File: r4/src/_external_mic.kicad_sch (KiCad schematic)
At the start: 145 parts, among them J27 , Q12 BSS84PW, Q13 BSS84PW, Q14 NX6008NBKW, Q15 NX3008NBKW, Q16 NX3008NBKW, Q17 NX3008NBKW, Q18 NX3008NBKW, Q19 NX3008NBKW, Q20 BSS84PW, Q21 BSS84PW, Q22 NX3008NBKW, Q23 NX3008NBKW, Q24 NX3008NBKW, Q25 BSS84PW, T17 , T18 , T19 , T20 , T21 , T22 , T23 , T24 , T25 , T26 , T27 , T28 , T29 , T30 , T31 , T32 , T33 , T34 , T35 , T36 , T37 , T38 , T41 , T43 , T44 , T45 , T46 , T47 , T48 , T49 , T50 , U17 74HC20, U18 THAT5173, U19 74HC74, U20 74HC132, U21 74HC4520, U22 74HC132, U23 THAT1580, U24 74HC688, U25 LM4562, U26 74HC688, U27 AD4005

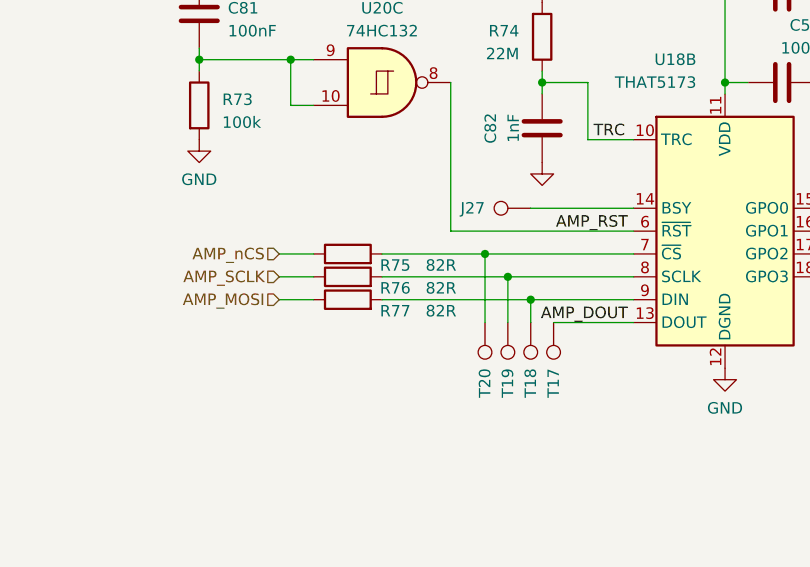
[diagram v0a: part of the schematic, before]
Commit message: Move SPI termination resistors to the source end of the bus (no electrical change, but clearer in schematic
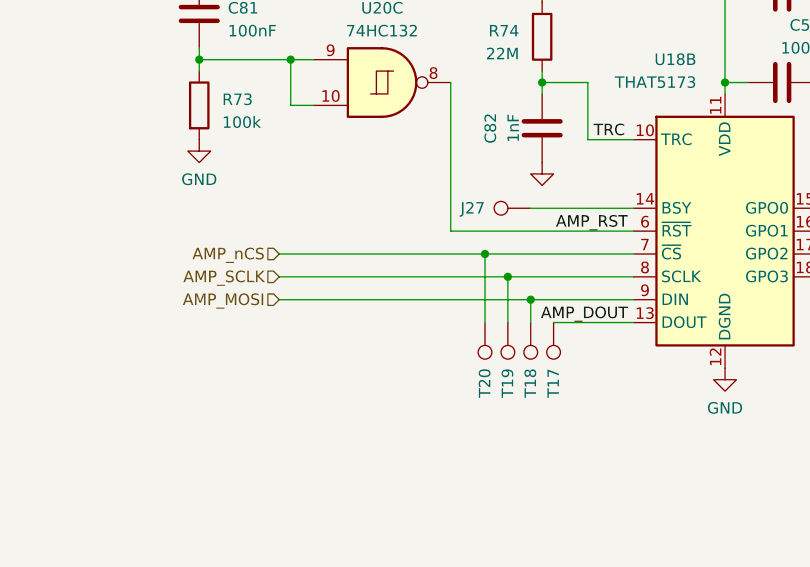
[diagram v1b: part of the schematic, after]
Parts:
- removed R75, R76, R77: 82R, Resistor_SMD:R_0402_1005Metric, symbol Device:R
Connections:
- net AMP_MOSI: now also T18.1, U18.9 (DIN)
- net AMP_SCLK: now also T19.1, U18.8 (SCLK)
- net AMP_nCS: now also T20.1, U18.7 (~{CS})
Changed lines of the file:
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@@
     (stroke (width 0) (type default))
   )
-  (wire (pts (xy 153.67 134.62) (xy 165.1 134.62))
+  (wire (pts (xy 142.24 134.62) (xy 165.1 134.62))
     (stroke (width 0) (type default))
   )
@@
     (stroke (width 0) (type default))
   )
-  (wire (pts (xy 153.67 137.16) (xy 167.64 137.16))
+  (wire (pts (xy 142.24 137.16) (xy 167.64 137.16))
     (stroke (width 0) (type default))
   )
@@
     (stroke (width 0) (type default))
   )
-  (wire (pts (xy 142.24 134.62) (xy 146.05 134.62))
-    (stroke (width 0) (type default))
-  )
   (wire (pts (xy 287.02 63.5) (xy 287.02 68.58))
     (stroke (width 0) (type default))
@@
     (stroke (width 0) (type default))
   )
-  (wire (pts (xy 142.24 137.16) (xy 146.05 137.16))
-    (stroke (width 0) (type default))
-  )
   (wire (pts (xy 466.09 154.94) (xy 463.55 154.94))
     (stroke (width 0) (type default))
@@
     (stroke (width 0) (type default))
   )
-  (wire (pts (xy 153.67 139.7) (xy 170.18 139.7))
+  (wire (pts (xy 142.24 139.7) (xy 170.18 139.7))
     (stroke (width 0) (type default))
   )
@@
     (stroke (width 0) (type default))
   )
-  (wire (pts (xy 142.24 139.7) (xy 146.05 139.7))
-    (stroke (width 0) (type default))
-  )
   (wire (pts (xy 274.32 351.79) (xy 294.64 351.79))
     (stroke (width 0) (type default))
@@
     )
   )
-  (symbol (lib_id "Device:R") (at 149.86 139.7 90) (unit 1)
-    (in_bom yes) (on_board yes) (dnp no)
-    (property "Reference" "R77" (at 156.845 140.97 90)
-      (effects (font (size 1.27 1.27)) (justify left))
-    )
-    (property "Value" "82R" (at 161.925 140.97 90)
-      (effects (font (size 1.27 1.27)) (justify left))
-    )
-    (property "Footprint" "Resistor_SMD:R_0402_1005Metric" (at 149.86 141.478 90)
-      (effects (font (size 1.27 1.27)) hide)
-    )
-    (property "Datasheet" "~" (at 149.86 139.7 0)
-      (effects (font (size 1.27 1.27)) hide)
-    )
-    (pin "1")
-    (pin "2")
-    (instances
-      (project "bugg-main-r4"
-        (path "/e3eb514f-6ce4-4abe-ba20-f82f0015628f/41f15edd-4583-4f5d-8a81-daeb7c83b416"
-          (reference "R77") (unit 1) (value "82R") (footprint "Resistor_SMD:R_0402_1005Metric")
-        )
-      )
-    )
-  )
   (symbol (lib_id "Device:R") (at 419.1 267.97 90) (unit 1)
     (in_bom yes) (on_board yes) (dnp no) (fields_autoplaced)
@@
     )
   )
-  (symbol (lib_id "Device:R") (at 149.86 134.62 90) (unit 1)
-    (in_bom yes) (on_board yes) (dnp no)
-    (property "Reference" "R75" (at 156.845 135.89 90)
-      (effects (font (size 1.27 1.27)) (justify left))
-    )
-    (property "Value" "82R" (at 161.925 135.89 90)
-      (effects (font (size 1.27 1.27)) (justify left))
-    )
-    (property "Footprint" "Resistor_SMD:R_0402_1005Metric" (at 149.86 136.398 90)
-      (effects (font (size 1.27 1.27)) hide)
-    )
-    (property "Datasheet" "~" (at 149.86 134.62 0)
-      (effects (font (size 1.27 1.27)) hide)
-    )
-    (pin "1")
-    (pin "2")
-    (instances
-      (project "bugg-main-r4"
-        (path "/e3eb514f-6ce4-4abe-ba20-f82f0015628f/41f15edd-4583-4f5d-8a81-daeb7c83b416"
-          (reference "R75") (unit 1) (value "82R") (footprint "Resistor_SMD:R_0402_1005Metric")
-        )
-      )
-    )
-  )
   (symbol (lib_id "Device:Q_PMOS_GSD") (at 110.49 228.6 0) (mirror x) (unit 1)
     (in_bom yes) (on_board yes) (dnp no)
@@
         )
       )
-    )
-  )
-  (symbol (lib_id "Device:R") (at 149.86 137.16 90) (unit 1)
-    (in_bom yes) (on_board yes) (dnp no)
-    (property "Reference" "R76" (at 156.845 138.43 90)
-      (effects (font (size 1.27 1.27)) (justify left))
-    )
-    (property "Value" "82R" (at 161.925 138.43 90)
-      (effects (font (size 1.27 1.27)) (justify left))
-    )
-    (property "Footprint" "Resistor_SMD:R_0402_1005Metric" (at 149.86 138.938 90)
-      (effects (font (size 1.27 1.27)) hide)
-    )
-    (property "Datasheet" "~" (at 149.86 137.16 0)
-      (effects (font (size 1.27 1.27)) hide)
-    )
-    (pin "1")
-    (pin "2")
-    (instances
-      (project "bugg-main-r4"
-        (path "/e3eb514f-6ce4-4abe-ba20-f82f0015628f/41f15edd-4583-4f5d-8a81-daeb7c83b416"
-          (reference "R76") (unit 1) (value "82R") (footprint "Resistor_SMD:R_0402_1005Metric")
-        )
-      )

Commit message: Remove unnecessary pull-down resistors from phantom switch circuits
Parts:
- removed R78, R80, R83: 100k, Resistor_SMD:R_0402_1005Metric, symbol Device:R
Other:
- moved on the sheet: C83, C84, Q15, Q16, Q17, Q18, Q19, Q20, Q21, Q22, Q23, Q24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

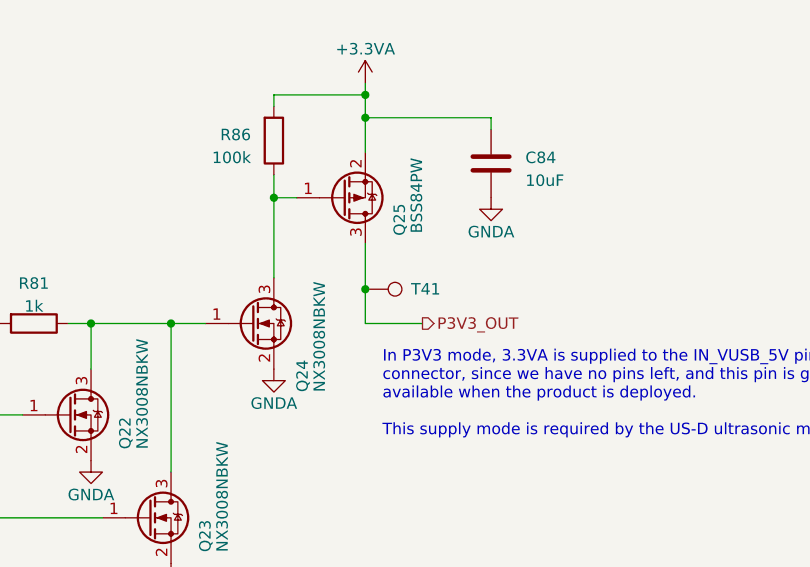
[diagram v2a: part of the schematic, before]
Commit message: Remove unnecessary testpoint
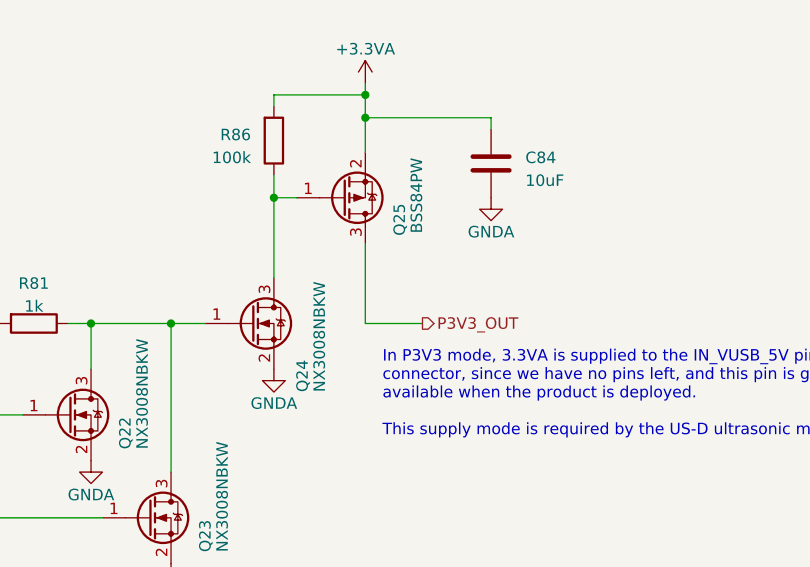
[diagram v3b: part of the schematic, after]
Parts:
- removed T41: (no value), TestPoint:TestPoint_Pad_D1.0mm, symbol Connector:TestPoint
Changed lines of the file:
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@@
   (junction (at 544.83 311.15) (diameter 0) (color 0 0 0 0)
-  )
-  (junction (at 288.29 231.14) (diameter 0) (color 0 0 0 0)
   )
   (junction (at 224.79 351.79) (diameter 0) (color 0 0 0 0)
@@
     (stroke (width 0) (type default))
   )
-  (wire (pts (xy 288.29 226.06) (xy 288.29 231.14))
+  (wire (pts (xy 288.29 226.06) (xy 288.29 234.95))
     (stroke (width 0) (type default))
   )
@@
   )
   (wire (pts (xy 431.8 95.25) (xy 431.8 96.52))
-    (stroke (width 0) (type default))
-  )
-  (wire (pts (xy 288.29 231.14) (xy 288.29 234.95))
     (stroke (width 0) (type default))
   )
@@
         )
       )
-    )
-  )
-  (symbol (lib_id "Connector:TestPoint") (at 288.29 231.14 270) (unit 1)
-    (in_bom yes) (on_board yes) (dnp no)
-    (property "Reference" "T41" (at 293.37 231.14 90)
-      (effects (font (size 1.27 1.27)) (justify left))
-    )
-    (property "Value" " " (at 293.37 232.41 90)
-      (effects (font (size 1.27 1.27)) (justify left))
-    )
-    (property "Footprint" "TestPoint:TestPoint_Pad_D1.0mm" (at 288.29 236.22 0)
-      (effects (font (size 1.27 1.27)) hide)
-    )
-    (property "Datasheet" "~" (at 288.29 236.22 0)
-      (effects (font (size 1.27 1.27)) hide)
-    )
-    (pin "1")
-    (instances
-      (project "bugg-main-r4"
-        (path "/e3eb514f-6ce4-4abe-ba20-f82f0015628f/41f15edd-4583-4f5d-8a81-daeb7c83b416"
-          (reference "T41") (unit 1) (value " ") (footprint "TestPoint:TestPoint_Pad_D1.0mm")
-        )
-      )

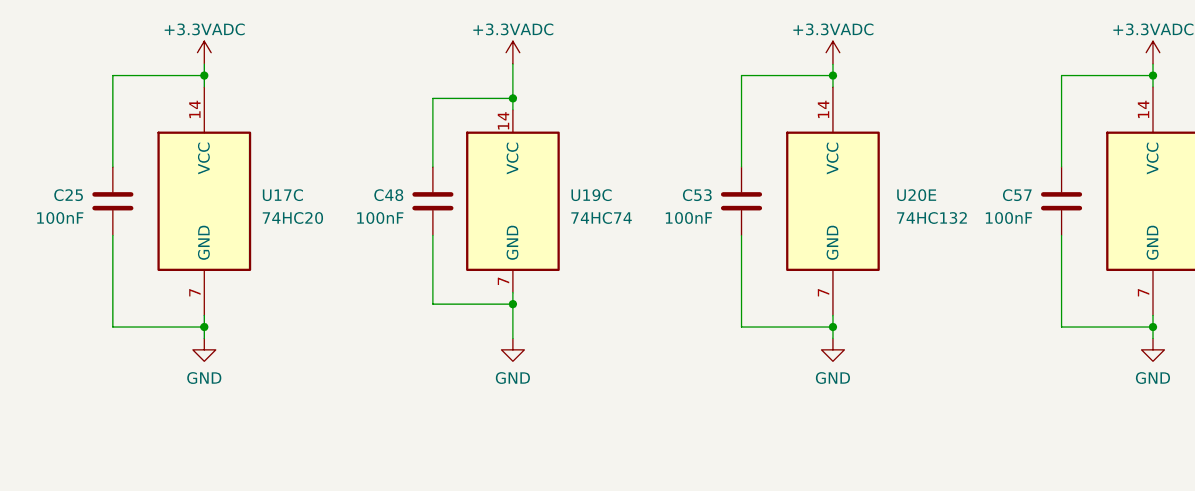
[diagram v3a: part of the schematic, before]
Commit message: Correct footprints for some accidentally-0201 decoupling caps
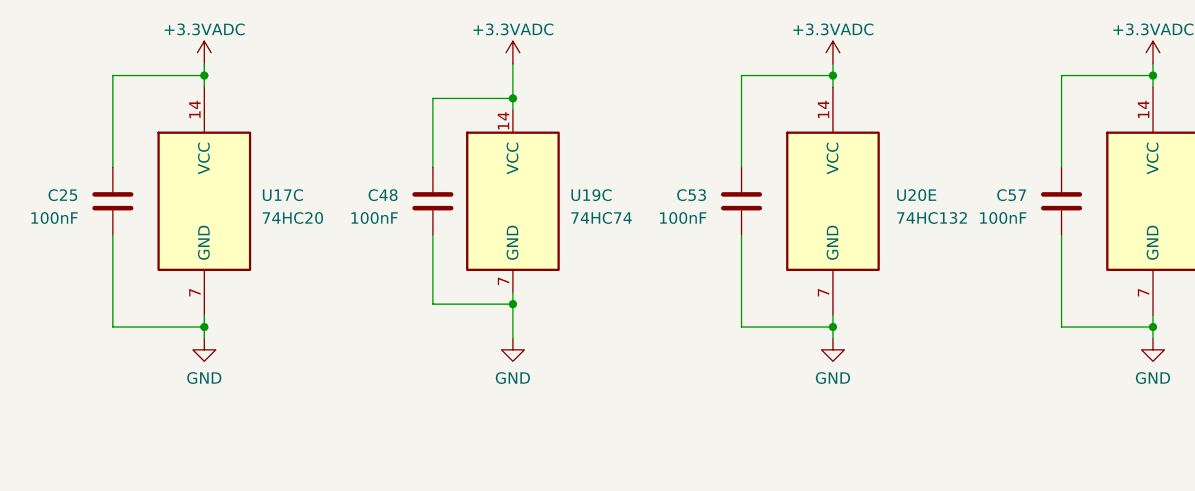
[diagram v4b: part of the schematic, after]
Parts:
- C25: footprint Capacitor_SMD:C_0603_1608Metric -> Capacitor_SMD:C_0402_1005Metric
- C51, C52, C53, C57: footprint Capacitor_SMD:C_0201_0603Metric -> Capacitor_SMD:C_0402_1005Metric
- D15: footprint Diode_SMD:D_SOD-123 -> Diode_SMD:D_SOD-323F
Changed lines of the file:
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@@
   (symbol (lib_id "Device:C") (at 68.58 35.56 0) (mirror x) (unit 1)
     (in_bom yes) (on_board yes) (dnp no) (fields_autoplaced)
-    (property "Reference" "C48" (at 65.405 34.925 0)
+    (property "Reference" "C48" (at 64.77 34.925 0)
       (effects (font (size 1.27 1.27)) (justify right))
     )
-    (property "Value" "100nF" (at 65.405 37.465 0)
+    (property "Value" "100nF" (at 64.77 37.465 0)
       (effects (font (size 1.27 1.27)) (justify right))
     )
@@
   (symbol (lib_id "Device:C") (at 138.43 35.56 0) (mirror x) (unit 1)
     (in_bom yes) (on_board yes) (dnp no) (fields_autoplaced)
-    (property "Reference" "C57" (at 135.255 34.925 0)
+    (property "Reference" "C57" (at 134.62 34.925 0)
       (effects (font (size 1.27 1.27)) (justify right))
     )
-    (property "Value" "100nF" (at 135.255 37.465 0)
+    (property "Value" "100nF" (at 134.62 37.465 0)
       (effects (font (size 1.27 1.27)) (justify right))
     )
-    (property "Footprint" "Capacitor_SMD:C_0201_0603Metric" (at 139.3952 31.75 0)
+    (property "Footprint" "Capacitor_SMD:C_0402_1005Metric" (at 139.3952 31.75 0)
       (effects (font (size 1.27 1.27)) hide)
     )
@@
       (project "bugg-main-r4"
         (path "/e3eb514f-6ce4-4abe-ba20-f82f0015628f/41f15edd-4583-4f5d-8a81-daeb7c83b416"
-          (reference "C57") (unit 1) (value "100nF") (footprint "Capacitor_SMD:C_0201_0603Metric")
+          (reference "C57") (unit 1) (value "100nF") (footprint "Capacitor_SMD:C_0402_1005Metric")
         )
       )
@@
   (symbol (lib_id "Device:C") (at 33.02 35.56 0) (mirror x) (unit 1)
     (in_bom yes) (on_board yes) (dnp no) (fields_autoplaced)
-    (property "Reference" "C25" (at 29.845 34.925 0)
+    (property "Reference" "C25" (at 29.21 34.925 0)
       (effects (font (size 1.27 1.27)) (justify right))
     )
-    (property "Value" "100nF" (at 29.845 37.465 0)
+    (property "Value" "100nF" (at 29.21 37.465 0)
       (effects (font (size 1.27 1.27)) (justify right))
     )
-    (property "Footprint" "Capacitor_SMD:C_0603_1608Metric" (at 33.9852 31.75 0)
+    (property "Footprint" "Capacitor_SMD:C_0402_1005Metric" (at 33.9852 31.75 0)
       (effects (font (size 1.27 1.27)) hide)
     )
@@
       (project "bugg-main-r4"
         (path "/e3eb514f-6ce4-4abe-ba20-f82f0015628f/41f15edd-4583-4f5d-8a81-daeb7c83b416"
-          (reference "C25") (unit 1) (value "100nF") (footprint "Capacitor_SMD:C_0603_1608Metric")
+          (reference "C25") (unit 1) (value "100nF") (footprint "Capacitor_SMD:C_0402_1005Metric")
         )
       )
@@
   (symbol (lib_id "Device:C") (at 102.87 35.56 0) (mirror x) (unit 1)
     (in_bom yes) (on_board yes) (dnp no) (fields_autoplaced)
-    (property "Reference" "C53" (at 99.695 34.925 0)
+    (property "Reference" "C53" (at 99.06 34.925 0)
       (effects (font (size 1.27 1.27)) (justify right))
     )
-    (property "Value" "100nF" (at 99.695 37.465 0)
+    (property "Value" "100nF" (at 99.06 37.465 0)
       (effects (font (size 1.27 1.27)) (justify right))
     )
-    (property "Footprint" "Capacitor_SMD:C_0201_0603Metric" (at 103.8352 31.75 0)
+    (property "Footprint" "Capacitor_SMD:C_0402_1005Metric" (at 103.8352 31.75 0)
       (effects (font (size 1.27 1.27)) hide)
     )
@@
       (project "bugg-main-r4"
         (path "/e3eb514f-6ce4-4abe-ba20-f82f0015628f/41f15edd-4583-4f5d-8a81-daeb7c83b416"
-          (reference "C53") (unit 1) (value "100nF") (footprint "Capacitor_SMD:C_0201_0603Metric")
+          (reference "C53") (unit 1) (value "100nF") (footprint "Capacitor_SMD:C_0402_1005Metric")
         )
       )
@@
       (effects (font (size 1.27 1.27)) (justify left))
     )
-    (property "Footprint" "Diode_SMD:D_SOD-123" (at 177.165 213.36 0)
+    (property "Footprint" "Diode_SMD:D_SOD-323F" (at 177.165 213.36 0)
       (effects (font (size 1.27 1.27)) hide)
     )
@@
       (project "bugg-main-r4"
         (path "/e3eb514f-6ce4-4abe-ba20-f82f0015628f/41f15edd-4583-4f5d-8a81-daeb7c83b416"
-          (reference "D15") (unit 1) (value "12V") (footprint "Diode_SMD:D_SOD-123")
+          (reference "D15") (unit 1) (value "12V") (footprint "Diode_SMD:D_SOD-323F")
         )
       )
@@
       (effects (font (size 1.27 1.27)))
     )
-    (property "Footprint" "Capacitor_SMD:C_0201_0603Metric" (at 194.31 114.6048 0)
+    (property "Footprint" "Capacitor_SMD:C_0402_1005Metric" (at 194.31 114.6048 0)
       (effects (font (size 1.27 1.27)) hide)
     )
@@
       (project "bugg-main-r4"
         (path "/e3eb514f-6ce4-4abe-ba20-f82f0015628f/41f15edd-4583-4f5d-8a81-daeb7c83b416"
-          (reference "C52") (unit 1) (value "100nF") (footprint "Capacitor_SMD:C_0201_0603Metric")
+          (reference "C52") (unit 1) (value "100nF") (footprint "Capacitor_SMD:C_0402_1005Metric")
         )
       )
@@
       (effects (font (size 1.27 1.27)))
     )
-    (property "Footprint" "Capacitor_SMD:C_0201_0603Metric" (at 194.31 104.4448 0)
+    (property "Footprint" "Capacitor_SMD:C_0402_1005Metric" (at 194.31 104.4448 0)
       (effects (font (size 1.27 1.27)) hide)
     )
@@
       (project "bugg-main-r4"
         (path "/e3eb514f-6ce4-4abe-ba20-f82f0015628f/41f15edd-4583-4f5d-8a81-daeb7c83b416"
-          (reference "C51") (unit 1) (value "100nF") (footprint "Capacitor_SMD:C_0201_0603Metric")
+          (reference "C51") (unit 1) (value "100nF") (footprint "Capacitor_SMD:C_0402_1005Metric")
         )
       )

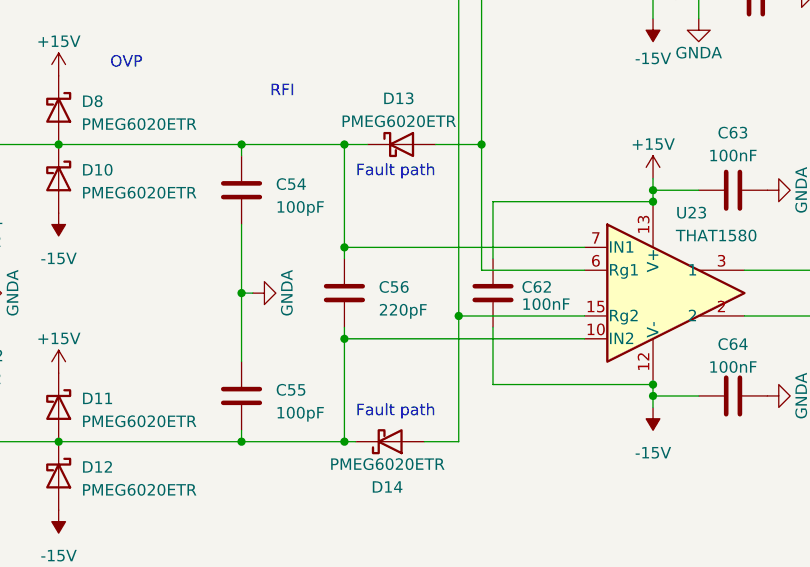
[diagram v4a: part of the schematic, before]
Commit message: Start routing the microphone signal path
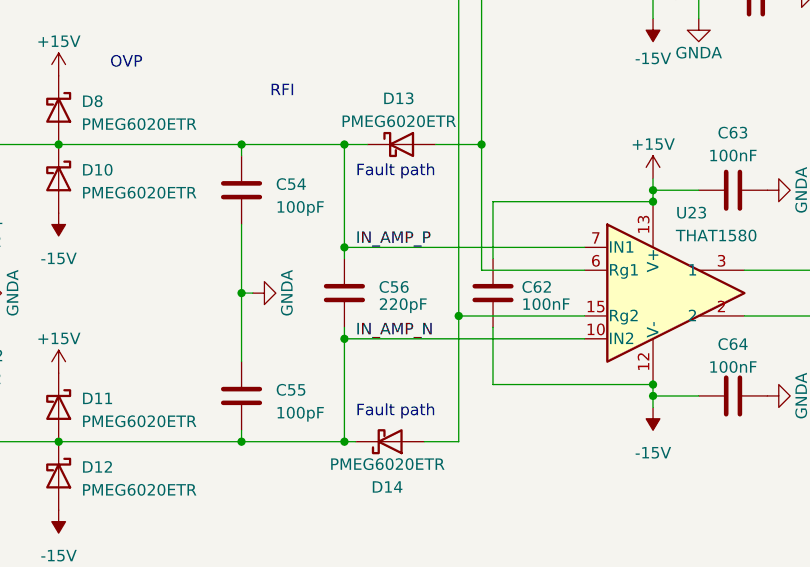
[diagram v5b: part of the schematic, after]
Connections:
- net IN_AMP_N: now reaches C55.1, C56.1, D11.2 (A), D12.1 (K), D14.1 (K), R48.2, R49.2, R52.2, T24.1, U23.10 (IN2)
- net IN_AMP_P: now reaches C54.2, C56.2, D10.1 (K), D13.1 (K), D8.2 (A), R47.2, R50.2, R51.1, T23.1, U23.7 (IN1)
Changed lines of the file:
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@@
+    (effects (font (size 1.27 1.27)) (justify left bottom))
+  )
+  (label "IN_AMP_N" (at 307.34 340.36 0) (fields_autoplaced)
     (effects (font (size 1.27 1.27)) (justify left bottom))
   )
@@
   (label "AMP_DOUT" (at 180.975 142.24 180) (fields_autoplaced)
     (effects (font (size 1.27 1.27)) (justify right bottom))
+  )
+  (label "IN_AMP_P" (at 307.34 330.2 0) (fields_autoplaced)
+    (effects (font (size 1.27 1.27)) (justify left bottom))
   )
   (label "!Qeq2" (at 392.43 104.14 180) (fields_autoplaced)
@@
       (effects (font (size 1.27 1.27)) (justify right))
     )
-    (property "Value" "220pF" (at 309.88 337.185 0)
-      (effects (font (size 1.27 1.27)) (justify right))
-    )
+    (property "Value" "220pF" (at 309.88 336.55 0)
+      (effects (font (size 1.27 1.27)) (justify right))
+    )
